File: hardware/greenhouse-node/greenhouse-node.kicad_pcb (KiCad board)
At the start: 2 copper layers, 90.2 x 69.8 mm, 54 parts, among them J1 Conn_01x12_Male, J2 Conn_01x02_Male, J3 Conn_01x02_Male, J4 Conn_01x02_Male, J5 Conn_01x04_Male, J6 RX_PinHeader_1x04_P2.54mm, J7 TX_PinHeader_1x04_P2.54mm, J8 Conn_01x02_Male, Q1 BC549C, Q2 BC549C, Q3 BC549C, Q4 IRF9530N, Q5 IRF530N, Q6 IRF9530N, Q7 IRF530N, Q8 BC549C, Q9 BC549C, U1 ATtiny84A-P, U2 L7805, U3 74HC595, Y1 8MHz

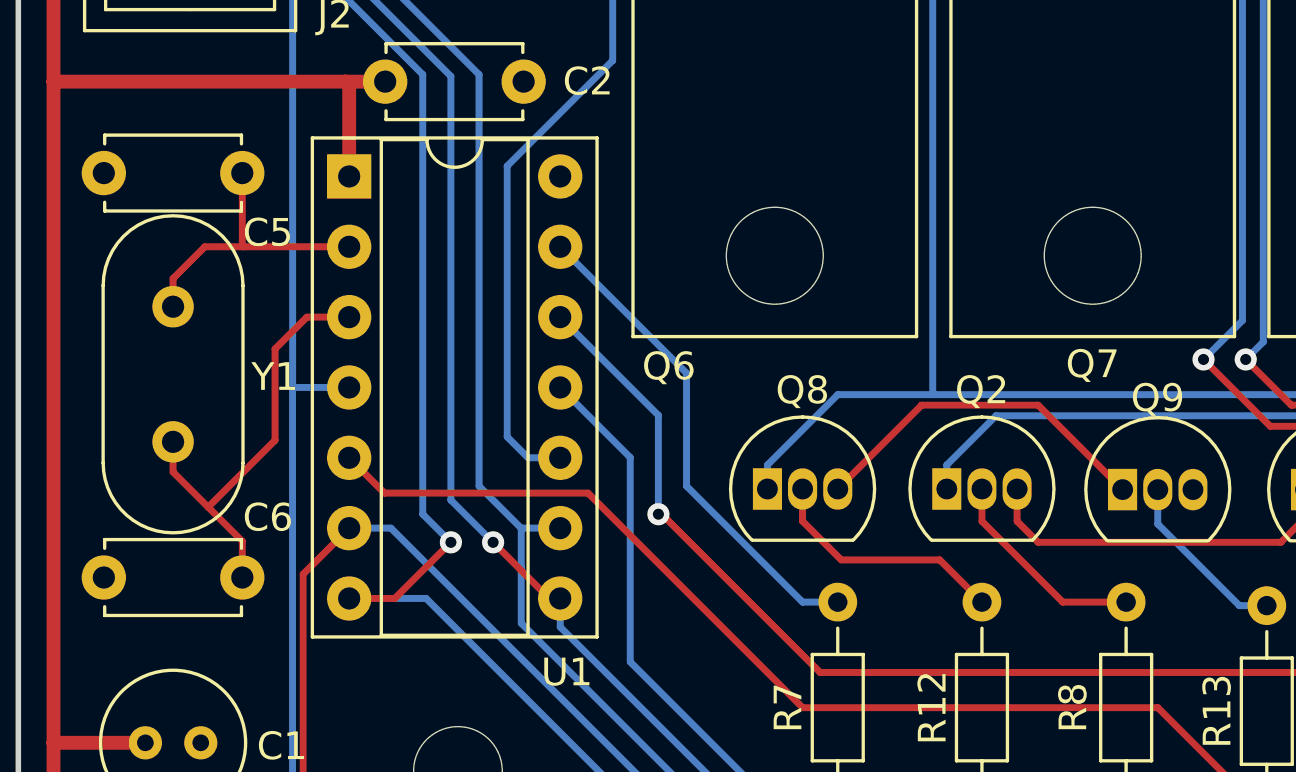
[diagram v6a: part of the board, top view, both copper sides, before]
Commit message: Widen crystal traces
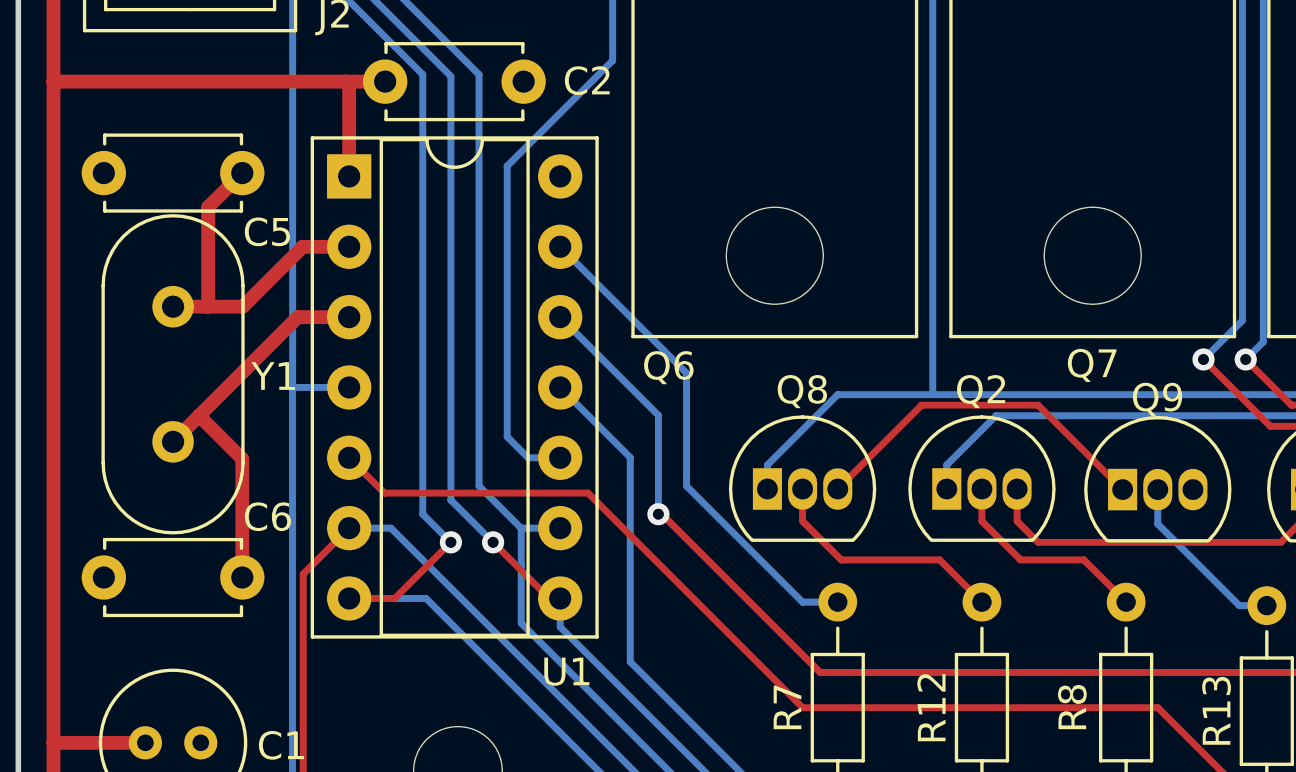
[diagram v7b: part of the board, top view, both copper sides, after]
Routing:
- net /XTAL1: track 10.5 -> 12.6 mm
- net /XTAL2: track 15.8 -> 14.7 mm
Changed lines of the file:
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@@
   (segment (start 134.366 58.166) (end 133.223 57.023) (width 0.25) (layer "B.Cu") (net 37))
   (segment (start 128.143 61.341) (end 127.127 62.357) (width 0.25) (layer "B.Cu") (net 37))
-  (segment (start 94.742 67.691) (end 97.663 70.612) (width 0.25) (layer "F.Cu") (net 38))
+  (segment (start 96.139 69.088) (end 98.425 69.088) (width 0.25) (layer "F.Cu") (net 38))
+  (segment (start 98.425 69.088) (end 99.949 70.612) (width 0.25) (layer "F.Cu") (net 38))
   (segment (start 94.742 66.527) (end 94.742 67.691) (width 0.25) (layer "F.Cu") (net 38))
-  (segment (start 97.663 70.612) (end 99.949 70.612) (width 0.25) (layer "F.Cu") (net 38))
+  (segment (start 94.742 67.691) (end 96.139 69.088) (width 0.25) (layer "F.Cu") (net 38))
   (segment (start 105.537 68.453) (end 106.426 67.564) (width 0.25) (layer "F.Cu") (net 39))
   (segment (start 96.012 66.527) (end 96.012 67.691) (width 0.25) (layer "F.Cu") (net 39))
@@
   (segment (start 146.3645 39.8985) (end 146.5785 39.8985) (width 0.5) (layer "F.Cu") (net 43))
   (segment (start 147.32 39.157) (end 146.5785 39.8985) (width 0.5) (layer "F.Cu") (net 43))
-  (segment (start 68.032 57.745) (end 68.067 57.78) (width 0.25) (layer "F.Cu") (net 44))
-  (segment (start 68.032 55.118) (end 68.032 57.745) (width 0.25) (layer "F.Cu") (net 44))
-  (segment (start 68.067 57.78) (end 71.892 57.78) (width 0.25) (layer "F.Cu") (net 44))
-  (segment (start 66.68 57.78) (end 68.067 57.78) (width 0.25) (layer "F.Cu") (net 44))
-  (segment (start 65.532 59.944) (end 65.532 58.928) (width 0.25) (layer "F.Cu") (net 44))
-  (segment (start 65.532 58.928) (end 66.68 57.78) (width 0.25) (layer "F.Cu") (net 44))
-  (segment (start 69.215 61.468) (end 69.215 64.77) (width 0.25) (layer "F.Cu") (net 45))
-  (segment (start 70.363 60.32) (end 69.215 61.468) (width 0.25) (layer "F.Cu") (net 45))
-  (segment (start 66.802 67.183) (end 68.032 68.413) (width 0.25) (layer "F.Cu") (net 45))
-  (segment (start 69.215 64.77) (end 66.802 67.183) (width 0.25) (layer "F.Cu") (net 45))
-  (segment (start 65.532 65.913) (end 66.802 67.183) (width 0.25) (layer "F.Cu") (net 45))
-  (segment (start 68.032 68.413) (end 68.032 69.723) (width 0.25) (layer "F.Cu") (net 45))
-  (segment (start 65.532 64.824) (end 65.532 65.913) (width 0.25) (layer "F.Cu") (net 45))
-  (segment (start 71.892 60.32) (end 70.363 60.32) (width 0.25) (layer "F.Cu") (net 45))
+  (segment (start 68.032 55.118) (end 66.802 56.348) (width 0.5) (layer "F.Cu") (net 44))
+  (segment (start 66.802 59.9186) (end 66.7766 59.944) (width 0.5) (layer "F.Cu") (net 44))
+  (segment (start 71.892 57.78) (end 70.2106 57.78) (width 0.5) (layer "F.Cu") (net 44))
+  (segment (start 66.7766 59.944) (end 65.532 59.944) (width 0.5) (layer "F.Cu") (net 44))
+  (segment (start 68.0466 59.944) (end 66.7766 59.944) (width 0.5) (layer "F.Cu") (net 44))
+  (segment (start 70.2106 57.78) (end 68.0466 59.944) (width 0.5) (layer "F.Cu") (net 44))
+  (segment (start 66.802 56.348) (end 66.802 59.9186) (width 0.5) (layer "F.Cu") (net 44))
+  (segment (start 68.032 69.723) (end 68.032 65.4412) (width 0.5) (layer "F.Cu") (net 45))
+  (segment (start 70.036 60.32) (end 71.892 60.32) (width 0.5) (layer "F.Cu") (net 45))
+  (segment (start 68.032 65.4412) (end 66.4734 63.8826) (width 0.5) (layer "F.Cu") (net 45))
+  (segment (start 66.4734 63.8826) (end 70.036 60.32) (width 0.5) (layer "F.Cu") (net 45))
+  (segment (start 65.532 64.824) (end 66.4734 63.8826) (width 0.5) (layer "F.Cu") (net 45))
   (zone (net 0) (net_name "") (layer "F.Cu") (hatch edge 0.508)
     (connect_pads (clearance 0))

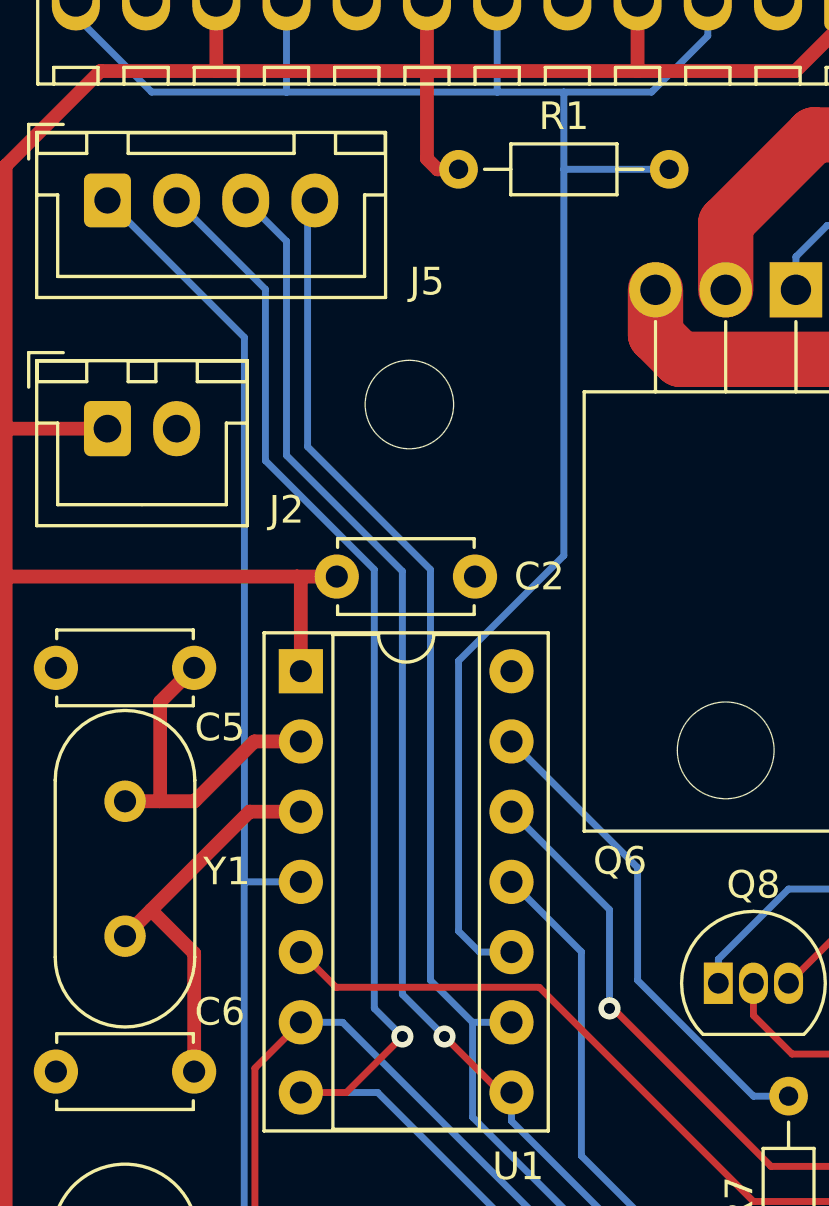
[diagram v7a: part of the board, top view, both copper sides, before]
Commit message: Improved ground return
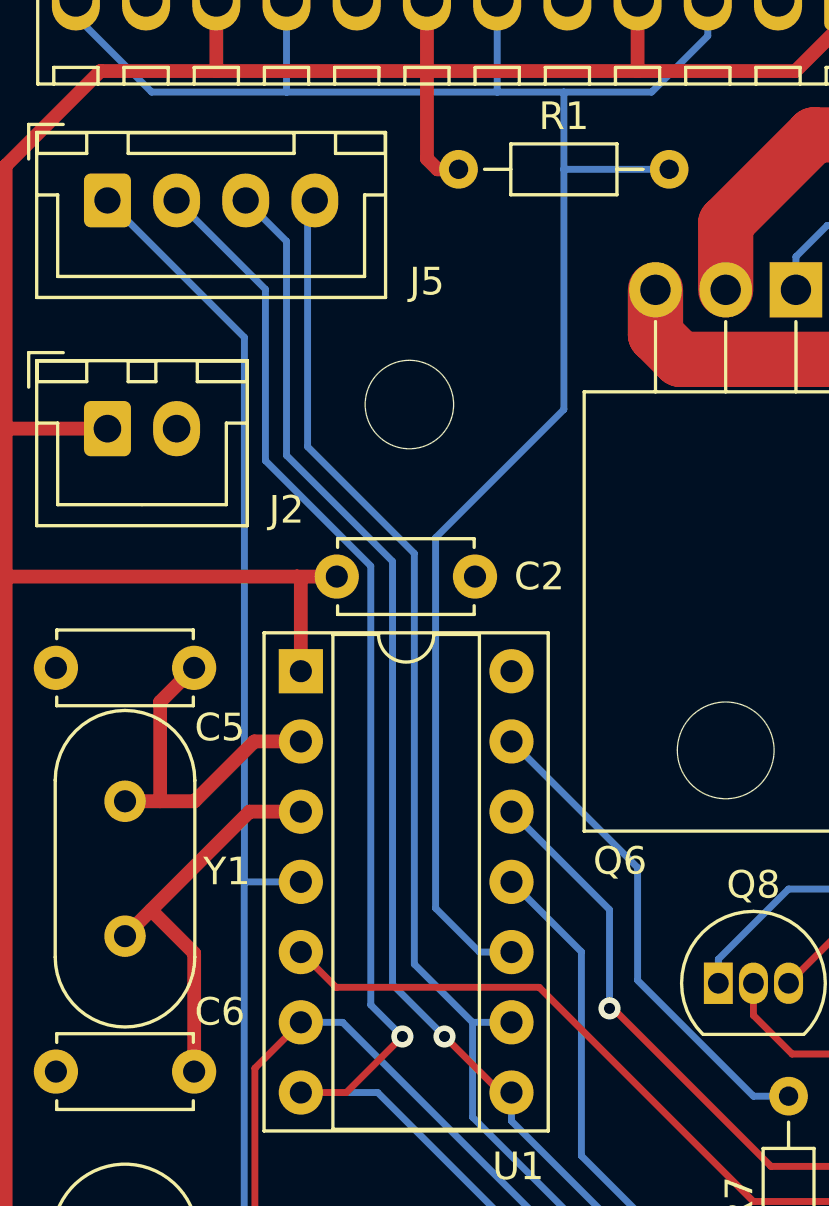
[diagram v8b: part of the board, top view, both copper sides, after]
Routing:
- net /OneWire: track 70.7 -> 71.4 mm
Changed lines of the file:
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@@
   (segment (start 104.149 33.8759) (end 102.4261 32.153) (width 0.25) (layer "B.Cu") (net 10))
   (segment (start 102.743 61.849) (end 104.149 60.443) (width 0.25) (layer "B.Cu") (net 10))
-  (segment (start 76.581 66.421) (end 78.105 67.945) (width 0.25) (layer "B.Cu") (net 11))
+  (segment (start 88.128 83.302) (end 88.128 81.397) (width 0.25) (layer "B.Cu") (net 11))
   (segment (start 72.397 38.21) (end 72.136 38.471) (width 0.25) (layer "B.Cu") (net 11))
-  (segment (start 88.128 83.302) (end 88.128 81.397) (width 0.25) (layer "B.Cu") (net 11))
   (segment (start 78.105 67.945) (end 78.11 67.94) (width 0.25) (layer "B.Cu") (net 11))
-  (segment (start 72.136 47.117) (end 76.581 51.562) (width 0.25) (layer "B.Cu") (net 11))
+  (segment (start 75.9968 65.8368) (end 78.105 67.945) (width 0.25) (layer "B.Cu") (net 11))
+  (segment (start 75.9968 50.9778) (end 75.9968 65.8368) (width 0.25) (layer "B.Cu") (net 11))
   (segment (start 78.105 71.374) (end 78.105 69.347) (width 0.25) (layer "B.Cu") (net 11))
-  (segment (start 76.581 51.562) (end 76.581 66.421) (width 0.25) (layer "B.Cu") (net 11))
   (segment (start 88.128 81.397) (end 78.105 71.374) (width 0.25) (layer "B.Cu") (net 11))
   (segment (start 78.11 67.94) (end 79.512 67.94) (width 0.25) (layer "B.Cu") (net 11))
+  (segment (start 72.136 47.117) (end 75.9968 50.9778) (width 0.25) (layer "B.Cu") (net 11))
   (segment (start 78.105 69.347) (end 78.105 67.945) (width 0.25) (layer "B.Cu") (net 11))
   (segment (start 72.136 38.471) (end 72.136 47.117) (width 0.25) (layer "B.Cu") (net 11))
@@
   (segment (start 73.538 70.48) (end 71.892 70.48) (width 0.25) (layer "F.Cu") (net 12))
   (via (at 75.565 68.453) (size 0.8) (drill 0.4) (layers "F.Cu" "B.Cu") (net 12))
+  (segment (start 70.612 47.625) (end 74.422 51.435) (width 0.25) (layer "B.Cu") (net 12))
   (segment (start 67.397 38.21) (end 70.612 41.425) (width 0.25) (layer "B.Cu") (net 12))
-  (segment (start 74.549 51.562) (end 74.549 67.437) (width 0.25) (layer "B.Cu") (net 12))
+  (segment (start 74.671 70.48) (end 83.048 78.857) (width 0.25) (layer "B.Cu") (net 12))
+  (segment (start 74.422 51.435) (end 74.422 67.31) (width 0.25) (layer "B.Cu") (net 12))
   (segment (start 70.612 41.425) (end 70.612 47.625) (width 0.25) (layer "B.Cu") (net 12))
-  (segment (start 74.671 70.48) (end 83.048 78.857) (width 0.25) (layer "B.Cu") (net 12))
-  (segment (start 74.549 67.437) (end 75.565 68.453) (width 0.25) (layer "B.Cu") (net 12))
   (segment (start 83.048 78.857) (end 83.048 83.302) (width 0.25) (layer "B.Cu") (net 12))
-  (segment (start 70.612 47.625) (end 74.549 51.562) (width 0.25) (layer "B.Cu") (net 12))
+  (segment (start 74.422 67.31) (end 75.565 68.453) (width 0.25) (layer "B.Cu") (net 12))
   (segment (start 71.892 70.48) (end 74.671 70.48) (width 0.25) (layer "B.Cu") (net 12))
   (segment (start 79.116 70.48) (end 79.512 70.48) (width 0.25) (layer "F.Cu") (net 13))
@@
   (via (at 77.089 68.453) (size 0.8) (drill 0.4) (layers "F.Cu" "B.Cu") (net 13))
   (segment (start 90.668 83.302) (end 90.668 82.667) (width 0.25) (layer "B.Cu") (net 13))
+  (segment (start 77.089 68.453) (end 75.2094 66.5734) (width 0.25) (layer "B.Cu") (net 13))
   (segment (start 71.374 47.433104) (end 71.374 39.687) (width 0.25) (layer "B.Cu") (net 13))
-  (segment (start 77.089 68.453) (end 75.565 66.929) (width 0.25) (layer "B.Cu") (net 13))
+  (segment (start 71.374 39.687) (end 69.897 38.21) (width 0.25) (layer "B.Cu") (net 13))
+  (segment (start 75.2094 66.5734) (end 75.2094 51.268504) (width 0.25) (layer "B.Cu") (net 13))
   (segment (start 90.668 82.667) (end 79.512 71.511) (width 0.25) (layer "B.Cu") (net 13))
-  (segment (start 75.565 66.929) (end 75.565 51.624104) (width 0.25) (layer "B.Cu") (net 13))
-  (segment (start 75.565 51.624104) (end 71.374 47.433104) (width 0.25) (layer "B.Cu") (net 13))
+  (segment (start 75.2094 51.268504) (end 71.374 47.433104) (width 0.25) (layer "B.Cu") (net 13))
   (segment (start 79.512 71.511) (end 79.512 70.48) (width 0.25) (layer "B.Cu") (net 13))
-  (segment (start 71.374 39.687) (end 69.897 38.21) (width 0.25) (layer "B.Cu") (net 13))
   (segment (start 71.892 67.94) (end 70.231 69.601) (width 0.25) (layer "F.Cu") (net 14))
   (segment (start 70.231 78.232) (end 67.056 81.407) (width 0.25) (layer "F.Cu") (net 14))
@@
   (segment (start 78.994 34.29) (end 71.374 34.29) (width 0.25) (layer "B.Cu") (net 15))
   (segment (start 86.614 32.258) (end 84.582 34.29) (width 0.25) (layer "B.Cu") (net 15))
+  (segment (start 76.767 63.813) (end 76.767 50.4108) (width 0.25) (layer "B.Cu") (net 15))
   (segment (start 66.4945 34.29) (end 63.754 31.5495) (width 0.25) (layer "B.Cu") (net 15))
   (segment (start 84.582 34.29) (end 81.407 34.29) (width 0.25) (layer "B.Cu") (net 15))
   (segment (start 81.407 37.084) (end 81.407 34.29) (width 0.25) (layer "B.Cu") (net 15))
+  (segment (start 86.614 30.968) (end 86.614 32.258) (width 0.25) (layer "B.Cu") (net 15))
   (segment (start 79.512 65.4) (end 78.354 65.4) (width 0.25) (layer "B.Cu") (net 15))
-  (segment (start 86.614 30.968) (end 86.614 32.258) (width 0.25) (layer "B.Cu") (net 15))
+  (segment (start 76.767 50.4108) (end 81.407 45.7708) (width 0.25) (layer "B.Cu") (net 15))
+  (segment (start 78.354 65.4) (end 76.767 63.813) (width 0.25) (layer "B.Cu") (net 15))
   (segment (start 81.407 34.29) (end 78.994 34.29) (width 0.25) (layer "B.Cu") (net 15))
-  (segment (start 81.407 51.054) (end 81.407 37.084) (width 0.25) (layer "B.Cu") (net 15))
   (segment (start 78.994 30.968) (end 78.994 34.29) (width 0.25) (layer "B.Cu") (net 15))
-  (segment (start 77.597 54.864) (end 81.407 51.054) (width 0.25) (layer "B.Cu") (net 15))
   (segment (start 66.4945 34.29) (end 71.374 34.29) (width 0.25) (layer "B.Cu") (net 15))
-  (segment (start 78.354 65.4) (end 77.597 64.643) (width 0.25) (layer "B.Cu") (net 15))
-  (segment (start 77.597 64.643) (end 77.597 54.864) (width 0.25) (layer "B.Cu") (net 15))
+  (segment (start 81.407 45.7708) (end 81.407 37.084) (width 0.25) (layer "B.Cu") (net 15))
   (segment (start 83.058 67.437) (end 83.185 67.437) (width 0.25) (layer "F.Cu") (net 16))
   (segment (start 83.185 67.437) (end 88.9 73.152) (width 0.25) (layer "F.Cu") (net 16))
